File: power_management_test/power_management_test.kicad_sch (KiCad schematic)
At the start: 52 parts, among them J1 Conn_01x02_Socket, J2 Conn_01x02_Socket, J3 Conn_01x02_Socket, J4 Conn_01x02_Socket, J5 Conn_01x06_Pin, J505 Conn_01x01_Socket, J6 Conn_01x02_Socket, J7 Conn_01x02_Socket, U503 INA169, U504 MCP6002T-E/OT

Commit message: Final Check
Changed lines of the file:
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@@
 				)
 				(justify left bottom)
-				(hide yes)
 			)
 		)
@@
 				)
 				(justify left bottom)
-				(hide yes)
-			)
-		)
+			)
+		)

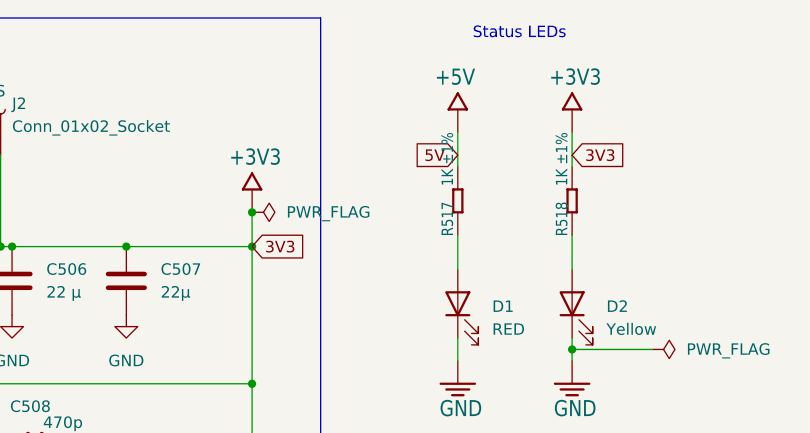
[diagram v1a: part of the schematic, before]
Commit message: Updated PM files and Schematics in the Support Board
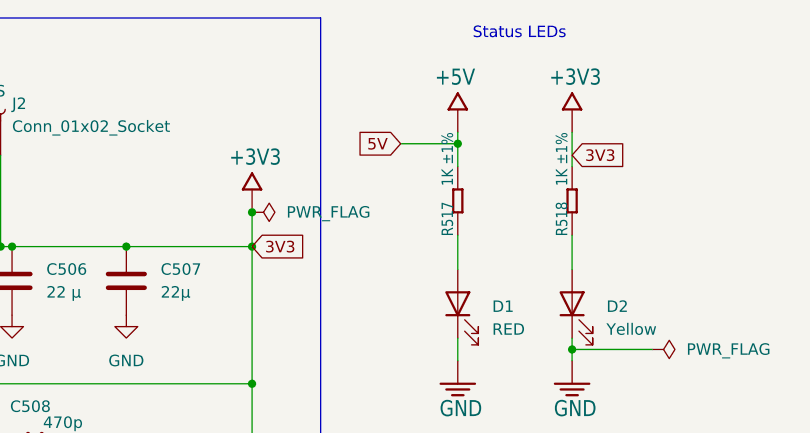
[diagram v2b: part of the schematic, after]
